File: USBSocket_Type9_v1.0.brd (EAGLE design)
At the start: 17.8 x 15.2 mm, 9 parts, among them CN4 USB4110-GF-A_REVB

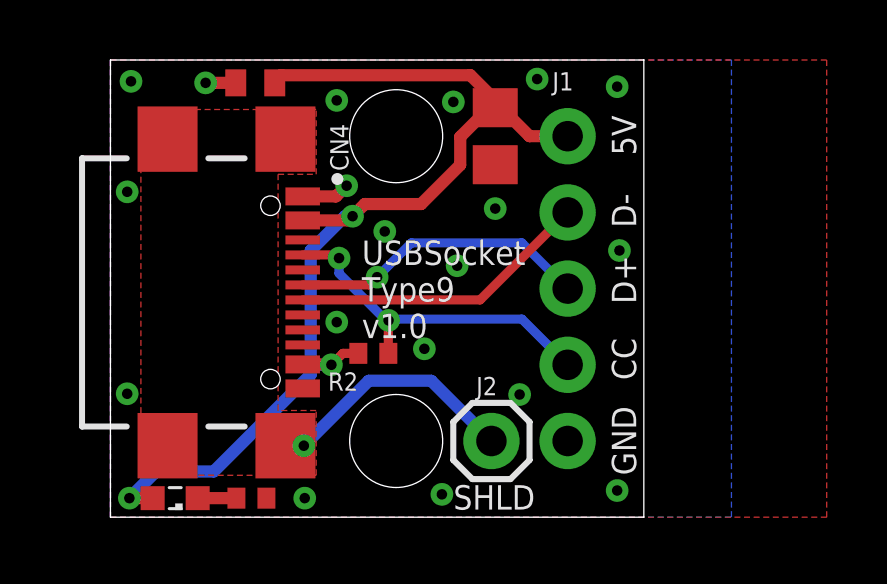
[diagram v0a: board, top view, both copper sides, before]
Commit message: Made type 9 board a bit shorter. Generated CAM files. Generated PNG preview.
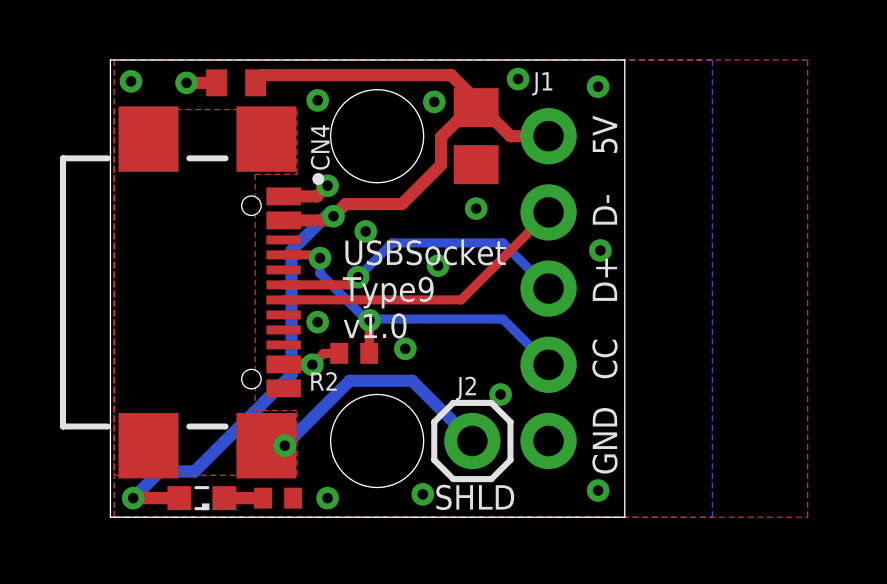
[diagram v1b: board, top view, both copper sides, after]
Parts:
- moved LED1 0.89 mm to (3.05, 0.64)
- moved R1 0.89 mm to (5.59, 0.64)
- moved LOGO1 0.64 mm to (20.4, 2.79)
- moved C1 0.63 mm to (12.2, 12.7)
- moved C2 0.63 mm to (4.19, 14.5)
- moved CN4 0.63 mm to (4.70, 7.49)
- moved J1 0.63 mm to (14.6, 12.7)
- moved J2 0.63 mm to (12.1, 2.54)
- moved R2 0.63 mm to (8.13, 5.46)
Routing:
- net GND: vias 19 -> 17
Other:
- board size 17.8 x 15.2 mm -> 17.1 x 15.2 mm
